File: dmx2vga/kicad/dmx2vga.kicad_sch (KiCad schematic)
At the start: 13 parts, among them J1 DMX In, J2 DMX Thru, J3 Programming Pins, SW1 RotaryEncoder_Switch, SW2 SW_Push, U1 Olimex_MOD-WIFI-ESP8266-DEV, U2 MAX485E

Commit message: add pcb
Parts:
- J1: footprint (none) -> Connector_Audio:Jack_XLR_Neutrik_NC3MAAV_Vertical
- J2: footprint (none) -> Connector_Audio:Jack_XLR_Neutrik_NC3FAAV2_Vertical
- J3: footprint (none) -> Connector_PinSocket_2.54mm:PinSocket_2x04_P2.54mm_Vertical
- JP1: footprint (none) -> Connector_PinSocket_2.54mm:PinSocket_1x02_P2.54mm_Vertical
- R1, R2, R3, R4: footprint (none) -> Resistor_SMD:R_1206_3216Metric
- SW1: footprint (none) -> Rotary_Encoder:RotaryEncoder_Alps_EC12E-Switch_Vertical_H20mm
- SW2: footprint (none) -> Button_Switch_THT:SW_PUSH-12mm
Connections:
- no-connect marks 1 -> 10

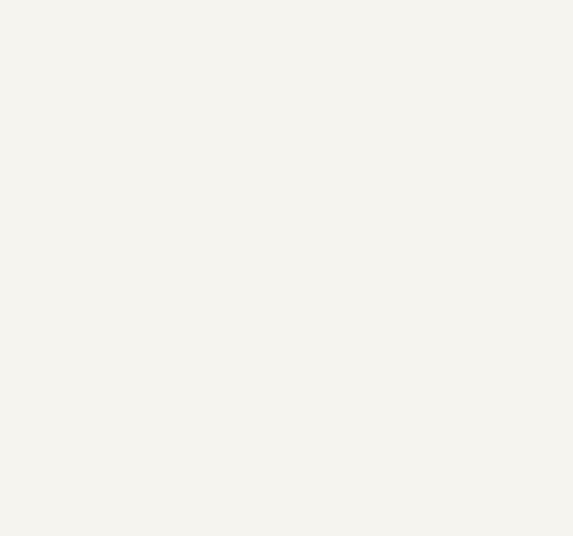
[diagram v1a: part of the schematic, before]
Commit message: feat(kicad): add icon; add vga connector
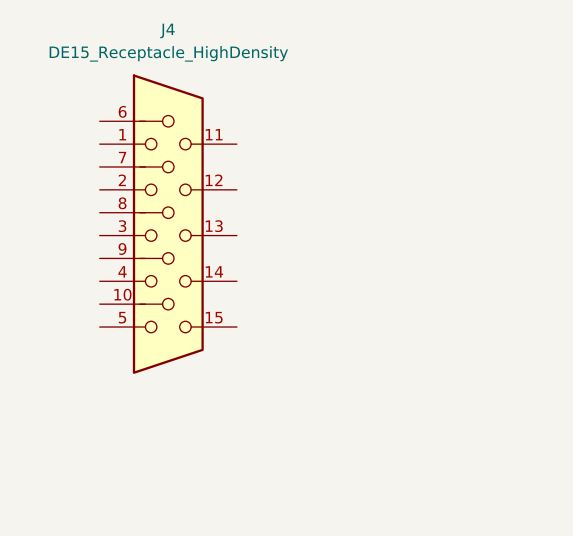
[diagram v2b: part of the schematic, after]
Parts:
- added J4: DE15_Receptacle_HighDensity, Connector_Dsub:DSUB-15-HD_Female_Horizontal_P2.29x1.98mm_EdgePinOffset8.35mm_Housed_MountingHolesOffset10.89mm, symbol Connector:DE15_Receptacle_HighDensity
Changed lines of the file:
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@@
+	)
+	(symbol
+		(lib_id "Connector:DE15_Receptacle_HighDensity")
+		(at 76.2 63.5 0)
+		(unit 1)
+		(exclude_from_sim no)
+		(in_bom yes)
+		(on_board yes)
+		(dnp no)
+		(fields_autoplaced yes)
+		(property "Reference" "J4"
+			(at 76.2 40.64 0)
+			(effects
+				(font
+					(size 1.27 1.27)
+				)
+			)
+		)
+		(property "Value" "DE15_Receptacle_HighDensity"
+			(at 76.2 43.18 0)
+			(effects
+				(font
+					(size 1.27 1.27)
+				)
+			)
+		)
+		(property "Footprint" "Connector_Dsub:DSUB-15-HD_Female_Horizontal_P2.29x1.98mm_EdgePinOffset8.35mm_Housed_MountingHolesOffset10.89mm"
+			(at 52.07 53.34 0)
+			(effects
+				(font
+					(size 1.27 1.27)
+				)
+				(hide yes)
+			)
+		)
+		(property "Datasheet" "~"
+			(at 52.07 53.34 0)
+			(effects
+				(font
+					(size 1.27 1.27)
+				)
+				(hide yes)
+			)
+		)
+		(property "Description" "15-pin female receptacle socket D-SUB connector, High density (3 columns), Triple Row, Generic, VGA-connector"
+			(at 76.2 63.5 0)
+			(effects
+				(font
+					(size 1.27 1.27)
+				)
+				(hide yes)
+			)
+		)
+		(pin "4"
+		)
+		(pin "15"
+		)
+		(pin "2"
+		)
+		(pin "11"
+		)
+		(pin "6"
+		)
+		(pin "14"
+		)
+		(pin "10"
+		)
+		(pin "7"
+		)
+		(pin "5"
+		)
+		(pin "3"
+		)
+		(pin "9"
+		)
+		(pin "12"
+		)
+		(pin "1"
+		)
+		(pin "13"
+		)
+		(pin "8"
+		)
+		(instances
+			(project ""
+				(path "/fa619e04-a5ac-414e-932d-fb70fe7b85b1"
+					(reference "J4")
+					(unit 1)
+				)
+			)
+		)
 	)
 	(symbol
